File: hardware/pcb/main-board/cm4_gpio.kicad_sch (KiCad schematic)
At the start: 14 parts, among them J402 CM4Lite SD Card, U402 RT9742SNGV

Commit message: rename CM4 to support RP link
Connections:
- net RX_FROM_SP_RP: no longer Module301.51 (GPIO15)
- net TX_TO_SP_RP: no longer Module301.55 (GPIO14)
- new net CM4_RX_FROM_SP_RP: Module301.51 (GPIO15)
- new net CM4_TX_TO_SP_RP: Module301.55 (GPIO14)

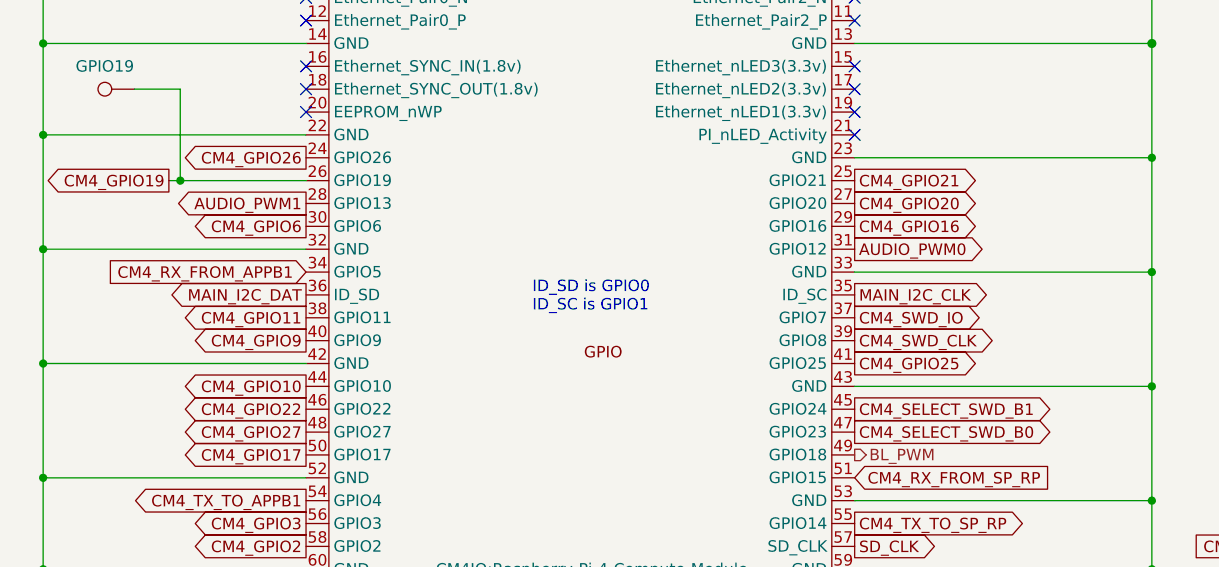
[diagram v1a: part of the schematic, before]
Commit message: move an SWD GPIO freeing up UART4 on the CM4. use that for talking to the appb Pico2
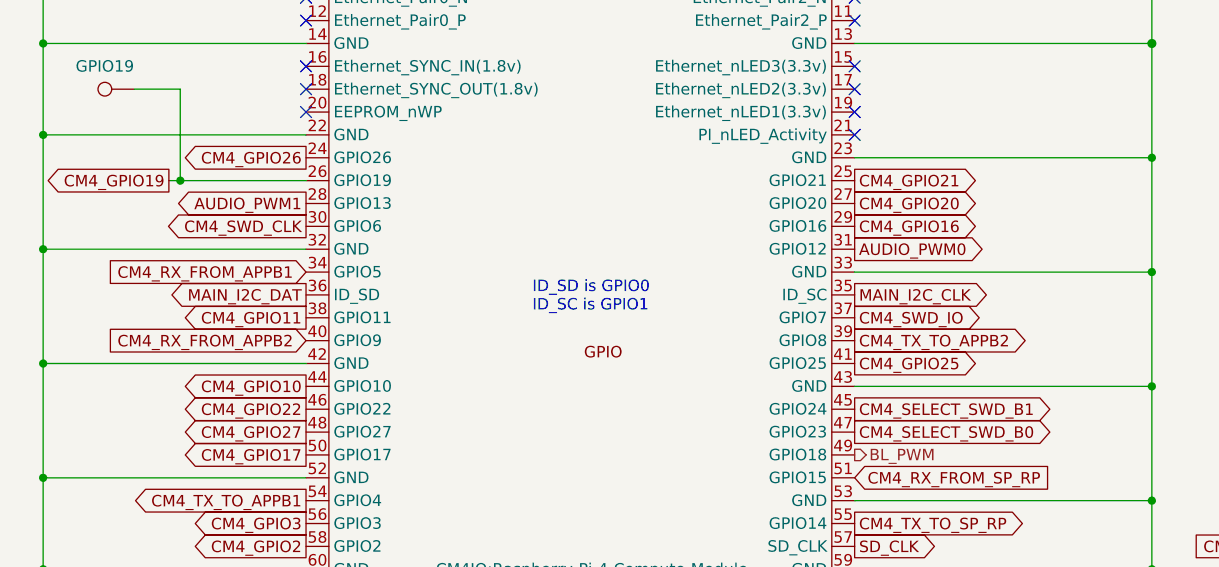
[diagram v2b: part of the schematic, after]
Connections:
- net CM4_GPIO6: no longer Module301.30 (GPIO6)
- net CM4_GPIO9: no longer Module301.40 (GPIO9)
- net CM4_SWD_CLK: now also Module301.30 (GPIO6); no longer Module301.39 (GPIO8)
- new net CM4_RX_FROM_APPB2: Module301.40 (GPIO9)
- new net CM4_TX_TO_APPB2: Module301.39 (GPIO8)
